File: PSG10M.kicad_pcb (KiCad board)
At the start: 2 copper layers, 80.8 x 96.1 mm, 164 parts, among them J1 Conn_Coaxial, J10 Conn_01x01_Pin, J11 Conn_01x01_Pin, J12 Conn_01x01_Pin, J13 Conn_01x01_Pin, J14 Conn_01x01_Pin, J15 Conn_01x01_Pin, J16 Conn_01x01_Pin, J2 USB_C_Receptacle_PowerOnly_6P, J3 Conn_01x02_Pin, J4 Conn_01x03_Pin, J5 Conn_01x04_Pin, J6 Conn_01x03_Pin, J7 Conn_01x01_Pin, J8 Conn_01x01_Pin, J9 Conn_01x01_Pin, Q1 J111, Q2 MMBF4393, Q5 BD679, Q6 BD680, SW1 RotaryEncoder_Switch, SW2 RotaryEncoder_Switch, U1 AD8933_module, U10 TL072, U11 LM7171, U12 L7805, U13 LMR62421XMF, U14 AP2204K-3.3, U15 L7905, U16 Screen to I2C, U17 Screen, U2 BluePill, U3 AD8039, U4 TL072, U5 AD5258BRM, U6 AD8039, U7 LM393LVDDFR, U8 FSA3157L6X, U9 FSA3157L6X

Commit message: T.
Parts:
- U17: footprint PSG:20x4 screen -> PSG:2x16_vertical
- moved U17 4.40 mm to (172.2, 128.1), turned to -90 degrees
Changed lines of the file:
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@@
 		)
 	)
-	(footprint "PSG:20x4 screen"
+	(footprint "PSG:2x16_vertical"
 		(layer "F.Cu")
-		(at 171.55 132.45 90)
+		(at 172.2125 128.1 -90)
 		(property "Reference" "U17"
-			(at 0 -0.5 90)
+			(at 0 -0.5 -90)
 			(unlocked yes)
 			(layer "F.SilkS")
@@
 		)
 		(property "Value" "Screen"
-			(at 0 1 90)
+			(at 0 1 -90)
 			(unlocked yes)
 			(layer "F.Fab")
@@
 			)
 		)
-		(property "Footprint" "PSG:20x4 screen"
-			(at 0 0 90)
+		(property "Footprint" "PSG:2x16_vertical"
+			(at 0 0 -90)
 			(unlocked yes)
 			(layer "F.Fab")
@@
 		)
 		(property "Datasheet" ""
-			(at 0 0 90)
+			(at 0 0 -90)
 			(unlocked yes)
 			(layer "F.Fab")
@@
 		)
 		(property "Description" ""
-			(at 0 0 90)
+			(at 0 0 -90)
 			(unlocked yes)
 			(layer "F.Fab")
@@
 		(attr smd)
 		(fp_rect
-			(start -41.95 -5.4)
-			(end 43.1 7.1)
+			(start -20 -3)
+			(end 20 0)
 			(stroke
 				(width 0.05)
@@
 		)
 		(fp_text user "${REFERENCE}"
-			(at 0 2.5 90)
+			(at 0 2.5 -90)
 			(unlocked yes)
 			(layer "F.Fab")
@@
 			)
 		)
-		(model "${KIPRJMOD}/LCD 20x4 Display.step"
+		(model "${KIPRJMOD}/LCD 16X2.STEP"
 			(offset
-				(xyz 0 0 25)
+				(xyz -15.5 0 64.5)
 			)
 			(scale
@@
 			)
 			(rotate
-				(xyz -90 0 0)
+				(xyz -90 0 180)
 			)
 		)

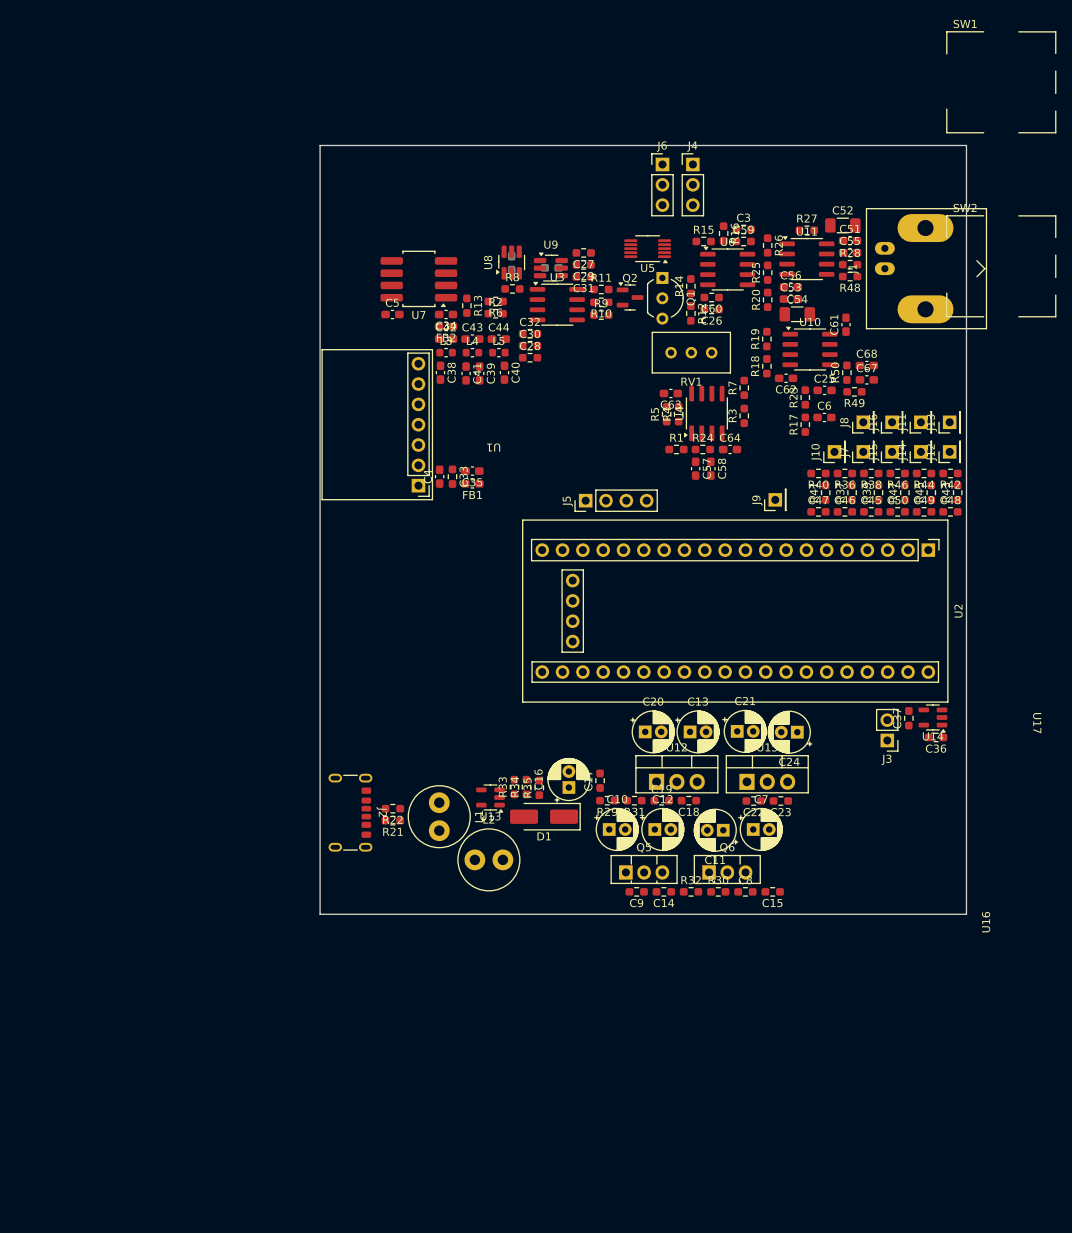
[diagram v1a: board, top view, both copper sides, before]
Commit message: SEPIC and CUK
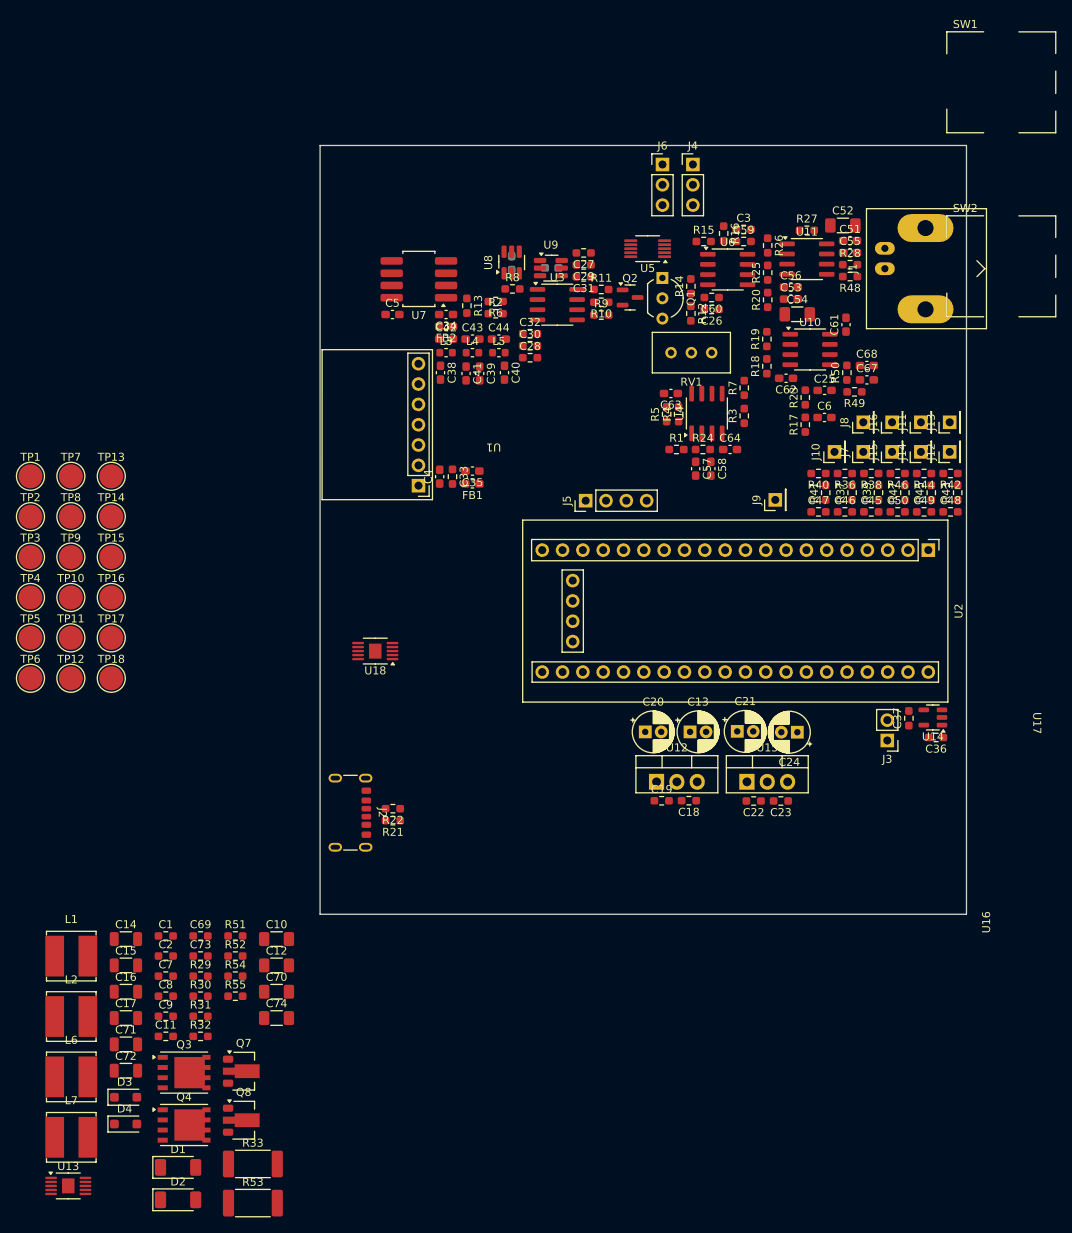
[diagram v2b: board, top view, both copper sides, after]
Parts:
- removed Q5: BD679, Package_TO_SOT_THT:TO-126-3_Vertical
- removed Q6: BD680, Package_TO_SOT_THT:TO-126-3_Vertical
- removed R34: 33k, Resistor_SMD:R_0603_1608Metric_Pad0.98x0.95mm_HandSolder
- removed R35: 249.9k, Resistor_SMD:R_0603_1608Metric_Pad0.98x0.95mm_HandSolder
- added C1: 470p, Resistor_SMD:R_0603_1608Metric_Pad0.98x0.95mm_HandSolder, F.Cu at (63.8, 154.7)
- added C2: 100n, Resistor_SMD:R_0603_1608Metric_Pad0.98x0.95mm_HandSolder, F.Cu at (63.8, 157.2)
- added C69: 1u, Resistor_SMD:R_0603_1608Metric_Pad0.98x0.95mm_HandSolder, F.Cu at (68.2, 154.7)
- added C70: 2u2, Resistor_SMD:R_1206_3216Metric_Pad1.30x1.75mm_HandSolder, F.Cu at (77.7, 161.7)
- added C71: 10u, Resistor_SMD:R_1206_3216Metric, F.Cu at (58.8, 168.3)
- added C72: 10u, Resistor_SMD:R_1206_3216Metric, F.Cu at (58.8, 171.6)
- added C73: 220n, Resistor_SMD:R_0603_1608Metric_Pad0.98x0.95mm_HandSolder, F.Cu at (68.2, 157.2)
- added C74: 2u2, Resistor_SMD:R_1206_3216Metric_Pad1.30x1.75mm_HandSolder, F.Cu at (77.7, 165.0)
- added D2: PMEG3020ER, Diode_SMD:D_SOD-128, F.Cu at (65.4, 187.7)
- added D3: BZT52H-C16,115, Diode_SMD:D_SOD-123F, F.Cu at (58.8, 174.9)
- added D4: BZT52H-C16,115, Diode_SMD:D_SOD-123F, F.Cu at (58.8, 178.2)
- added L6: 4.7u, Inductor_SMD:L_Bourns_SRN6045TA, F.Cu at (52.0, 172.3)
- added L7: 4.7u, Inductor_SMD:L_Bourns_SRN6045TA, F.Cu at (52.0, 179.9)
- added Q3: NTMFS4937N, Package_SO:PowerPAK_SO-8_Single, F.Cu at (66.1, 171.8)
- added Q4: NTMFS4937N, Package_SO:PowerPAK_SO-8_Single, F.Cu at (66.1, 178.3)
- added Q7: PBSS4360X, Package_TO_SOT_SMD:SOT-89-3, F.Cu at (73.5, 171.6)
- added Q8: PBSS5240X, Package_TO_SOT_SMD:SOT-89-3, F.Cu at (73.5, 177.7)
- added R51: 220k, Resistor_SMD:R_0603_1608Metric_Pad0.98x0.95mm_HandSolder, F.Cu at (72.5, 154.7)
- added R52: 10, Resistor_SMD:R_0603_1608Metric_Pad0.98x0.95mm_HandSolder, F.Cu at (72.5, 157.2)
- added R53: 10m, Resistor_SMD:R_2512_6332Metric_Pad1.40x3.35mm_HandSolder, F.Cu at (74.7, 188.1)
- added R54: 10k, Resistor_SMD:R_0603_1608Metric_Pad0.98x0.95mm_HandSolder, F.Cu at (72.5, 159.7)
- added R55: 1k, Resistor_SMD:R_0603_1608Metric_Pad0.98x0.95mm_HandSolder, F.Cu at (72.5, 162.2)
- added TP1: TestPoint, TestPoint:TestPoint_Pad_D3.0mm, F.Cu at (46.9, 97.2)
- added TP10: TestPoint, TestPoint:TestPoint_Pad_D3.0mm, F.Cu at (52.0, 112.4)
- added TP11: TestPoint, TestPoint:TestPoint_Pad_D3.0mm, F.Cu at (52.0, 117.5)
- added TP12: TestPoint, TestPoint:TestPoint_Pad_D3.0mm, F.Cu at (52.0, 122.5)
- added TP13: TestPoint, TestPoint:TestPoint_Pad_D3.0mm, F.Cu at (57.0, 97.2)
- added TP14: TestPoint, TestPoint:TestPoint_Pad_D3.0mm, F.Cu at (57.0, 102.3)
- added TP15: TestPoint, TestPoint:TestPoint_Pad_D3.0mm, F.Cu at (57.0, 107.3)
- added TP16: TestPoint, TestPoint:TestPoint_Pad_D3.0mm, F.Cu at (57.0, 112.4)
- added TP17: TestPoint, TestPoint:TestPoint_Pad_D3.0mm, F.Cu at (57.0, 117.5)
- added TP18: TestPoint, TestPoint:TestPoint_Pad_D3.0mm, F.Cu at (57.0, 122.5)
- added TP2: TestPoint, TestPoint:TestPoint_Pad_D3.0mm, F.Cu at (46.9, 102.3)
- added TP3: TestPoint, TestPoint:TestPoint_Pad_D3.0mm, F.Cu at (46.9, 107.3)
- added TP4: TestPoint, TestPoint:TestPoint_Pad_D3.0mm, F.Cu at (46.9, 112.4)
- added TP5: TestPoint, TestPoint:TestPoint_Pad_D3.0mm, F.Cu at (46.9, 117.5)
- added TP6: TestPoint, TestPoint:TestPoint_Pad_D3.0mm, F.Cu at (46.9, 122.5)
- added TP7: TestPoint, TestPoint:TestPoint_Pad_D3.0mm, F.Cu at (52.0, 97.2)
- added TP8: TestPoint, TestPoint:TestPoint_Pad_D3.0mm, F.Cu at (52.0, 102.3)
- added TP9: TestPoint, TestPoint:TestPoint_Pad_D3.0mm, F.Cu at (52.0, 107.3)
- added U18: TPS40210, Package_SO:HVSSOP-10-1EP_3x3mm_P0.5mm_EP1.57x1.88mm, F.Cu at (90.0, 119.1)
- C10, C12: value 47u -> 2u2; footprint Capacitor_THT:CP_Radial_D5.0mm_P2.00mm -> Resistor_SMD:R_1206_3216Metric_Pad1.30x1.75mm_HandSolder
- C11: value 47u -> 1u; footprint Capacitor_THT:CP_Radial_D5.0mm_P2.00mm -> Resistor_SMD:R_0603_1608Metric_Pad0.98x0.95mm_HandSolder
- C14, C15, C17: value 1u -> 10u; footprint Resistor_SMD:R_0603_1608Metric_Pad0.98x0.95mm_HandSolder -> Resistor_SMD:R_1206_3216Metric
- C16: value 47u -> 10u; footprint Capacitor_THT:CP_Radial_D5.0mm_P2.00mm -> Resistor_SMD:R_1206_3216Metric
- C7: value 47u -> 470p; footprint Capacitor_THT:CP_Radial_D5.0mm_P2.00mm -> Resistor_SMD:R_0603_1608Metric_Pad0.98x0.95mm_HandSolder
- C8: value 1u -> 100n
- C9: value 1u -> 220n
- D1: value SK16 -> PMEG3020ER; footprint Diode_SMD:D_SMA_Handsoldering -> Diode_SMD:D_SOD-128
- L1, L2: footprint Inductor_THT:L_Radial_D7.5mm_P3.50mm_Fastron_07P -> Inductor_SMD:L_Bourns_SRN6045TA
- R2, R6: value 10k -> 100
- R30: value 1k -> 220k
- R31: value 10k -> 10
- R33: value 33k -> 10m; footprint Resistor_SMD:R_0603_1608Metric_Pad0.98x0.95mm_HandSolder -> Resistor_SMD:R_2512_6332Metric_Pad1.40x3.35mm_HandSolder
- R8: value 33k -> 330
- U13: value LMR62421XMF -> TPS40210; footprint Package_TO_SOT_SMD:SOT-23-5 -> Package_SO:HVSSOP-10-1EP_3x3mm_P0.5mm_EP1.57x1.88mm
- moved C15 81.4 mm to (58.8, 158.4), turned to 0 degrees
- moved C7 75.7 mm to (63.8, 159.7)
- moved C11 74.3 mm to (63.8, 167.3), turned to 0 degrees
- moved C8 73.6 mm to (63.8, 162.2)
- moved U13 71.7 mm to (51.6, 186.0), turned to 0 degrees
- moved C14 67.5 mm to (58.8, 155.1), turned to 0 degrees
- moved C17 66.3 mm to (58.8, 165.0), turned to 0 degrees
- moved R30 66.0 mm to (68.2, 162.2)
- moved R32 63.9 mm to (68.2, 167.3)
- moved D1 63.4 mm to (65.4, 183.6), turned to 0 degrees
- moved C16 61.0 mm to (58.8, 161.7), turned to 0 degrees
- moved C9 60.9 mm to (63.8, 164.8), turned to 0 degrees
- moved R31 60.6 mm to (68.2, 164.8), turned to 0 degrees
- moved R33 57.3 mm to (74.7, 183.2), turned to 0 degrees
- moved R29 55.4 mm to (68.2, 159.7), turned to 0 degrees
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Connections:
- C10 pad 1: Net-(Q5-B) -> GND
- C10 pad 2: GND -> -15.3V
- C11 pad 1: GND -> +VBPC
- C11 pad 2: Net-(Q6-B) -> GND
- C12 pad 1: +16.5V -> Net-(Q4-D)
- C12 pad 2: GND -> Net-(D1-A)
- C14 pad 1: +16.5V -> -17V
- C15 pad 1: -16.5V -> -17V
- C16 pad 1: +20V -> +VBUS
- C17 pad 1: +20V -> +VBUS
- C19 pad 1: +16.5V -> +15.3V
- C20 pad 1: +16.5V -> +15.3V
- C21 pad 2: -16.5V -> -15.3V
- C22 pad 1: -16.5V -> -15.3V
- C36 pad 1: +5V -> +VBUS
- C7 pad 1: GND -> Net-(U13-RC)
- C7 pad 2: -16.5V -> GND
- C8 pad 1: +20V -> Net-(U13-SS)
- C9 pad 1: +20V -> Net-(D4-A)
- D1 pad 1: +20V -> GND
- L1 pad 2: Net-(L1-Pad2) -> Net-(Q4-D)
- L2 pad 1: Net-(L1-Pad2) -> Net-(D1-A)
- L2 pad 2: Net-(D1-A) -> -17V
- R29 pad 1: Net-(Q5-B) -> Net-(D4-A)
- R29 pad 2: +20V -> -17V
- R30 pad 1: Net-(Q6-B) -> Net-(U13-RC)
- R30 pad 2: +20V -> +VBUS
- R31 pad 1: GND -> Net-(Q4-G)
- R31 pad 2: Net-(Q5-B) -> Net-(U13-GDRV)
- R32 pad 1: GND -> Net-(Q4-S-Pad1)
- R32 pad 2: Net-(Q6-B) -> Net-(U13-ISNS)
- R33 pad 1: GND -> Net-(Q4-S-Pad1)
- R33 pad 2: Net-(U13-FB) -> GND
- U12 pad 1: +16.5V -> +15.3V
- U13 pad 1: Net-(D1-A) -> Net-(U13-RC)
- U13 pad 2: GND -> Net-(U13-SS)
- U13 pad 3: Net-(U13-FB) -> GND
- U13 pad 4: +VBUS -> unconnected-(U13-COMP-Pad4)
- U13 pad 5: +VBUS -> unconnected-(U13-FB-Pad5)
- U14 pad 1: +5V -> +VBUS
- U14 pad 3: +5V -> +VBUS
- U15 pad 2: -16.5V -> -15.3V
- U2 pad 10: unconnected-(U2-PA15-Pad10) -> Net-(U2-PA15)
- U2 pad 11: unconnected-(U2-PB3-Pad11) -> Net-(U2-PB3)
- U2 pad 12: unconnected-(U2-PB4-Pad12) -> Net-(U2-PB4)
- U2 pad 13: unconnected-(U2-PB5-Pad13) -> Net-(U2-PB5)
- U2 pad 21: unconnected-(U2-VBat-Pad21) -> Net-(U2-VBat)
- U2 pad 24: unconnected-(U2-PC15-Pad24) -> Net-(U2-PC15)
- U2 pad 28: unconnected-(U2-PA3-Pad28) -> Net-(U2-PA3)
- U2 pad 29: unconnected-(U2-PA4-Pad29) -> Net-(U2-PA4)
- U2 pad 31: unconnected-(U2-PA6-Pad31) -> Net-(U2-PA6)
- U2 pad 34: unconnected-(U2-PB1-Pad34) -> Net-(U2-PB1)
- U2 pad 35: unconnected-(U2-PB10-Pad35) -> Net-(U2-PB10)
- U2 pad 36: unconnected-(U2-PB11-Pad36) -> Net-(U2-PB11)
- U2 pad 37: unconnected-(U2-RST-Pad37) -> Net-(U2-RST)
- U2 pad 42: unconnected-(U2-SWCLK-Pad42) -> Net-(U2-SWCLK)
- U2 pad 43: unconnected-(U2-SWIO-Pad43) -> Net-(U2-SWIO)
- U2 pad 7: unconnected-(U2-PA10-Pad7) -> Net-(U2-PA10)
- U2 pad 8: unconnected-(U2-PA11-Pad8) -> Net-(U2-PA11)
- U2 pad 9: unconnected-(U2-PA12-Pad9) -> Net-(U2-PA12)
